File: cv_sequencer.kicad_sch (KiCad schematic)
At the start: 27 parts, among them J10 3096_USBC_RA_SMD, J11 4005_SWD_Header, J9 3086_Connector_Eurorack_Power, U1 3097_TFT_Display_SPI, U2 3093_MIC5225_3v3, U3 4002_RP2040, Y1 4004-Crystal-12MHz_GND24

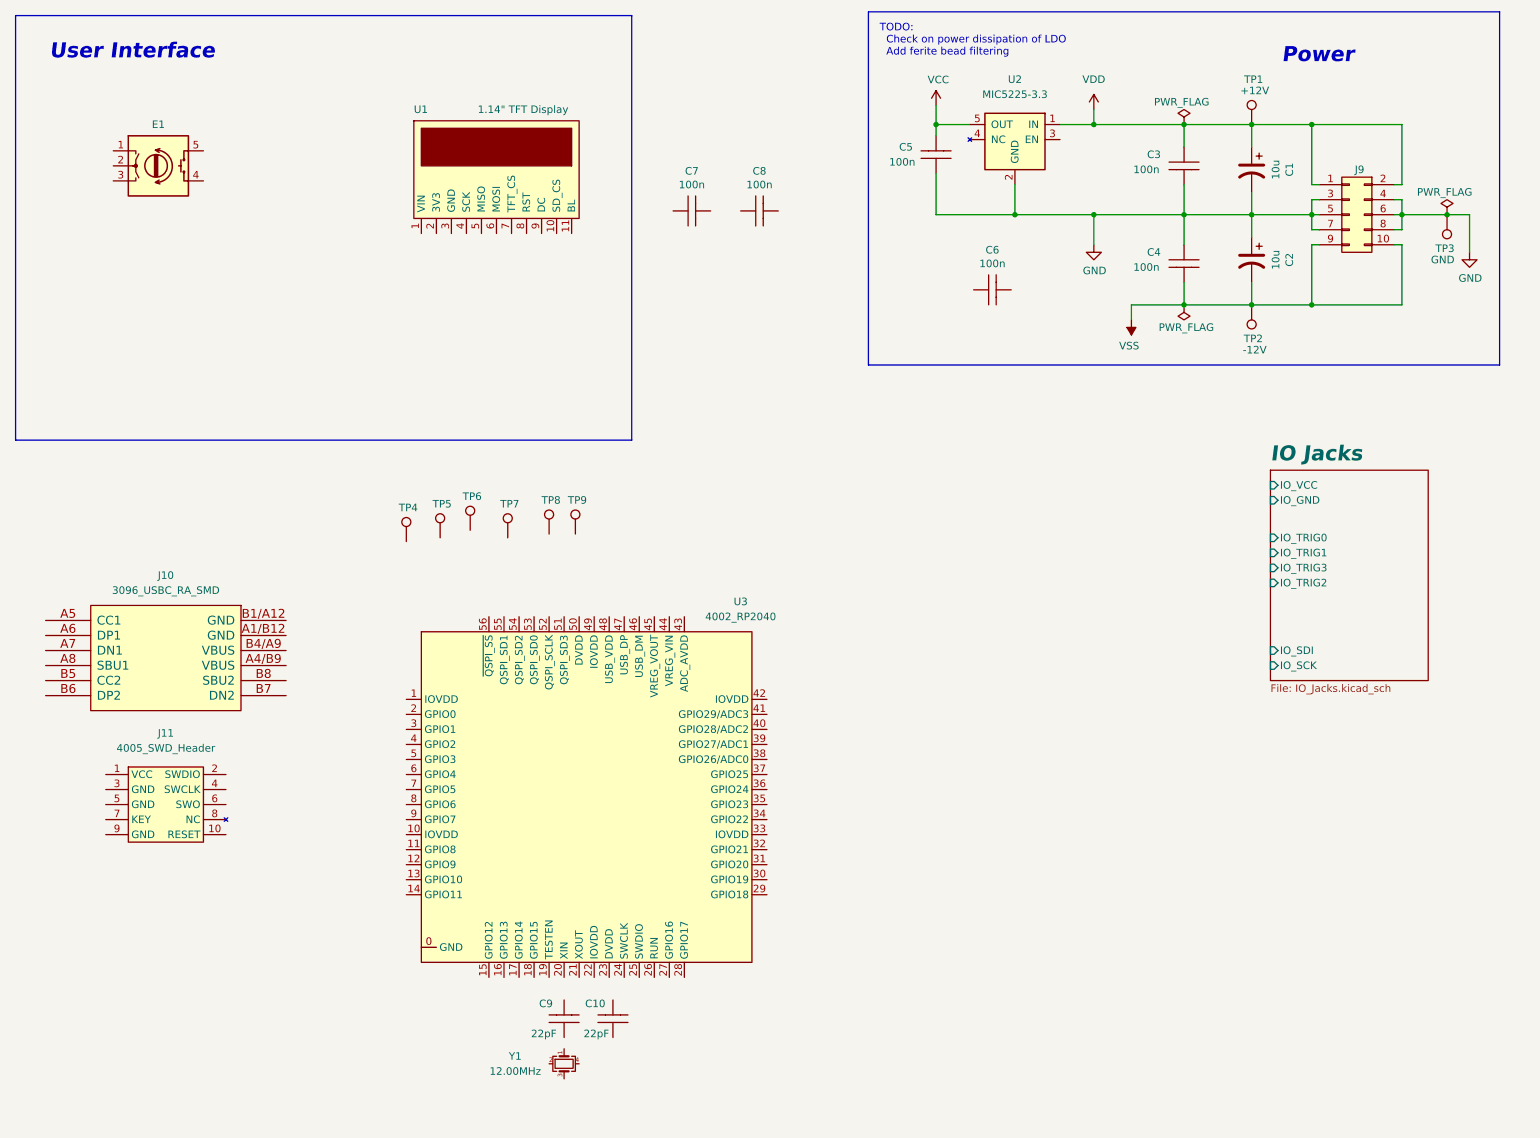
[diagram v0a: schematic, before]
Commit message: fleshed out a lot of the MCU circuitry
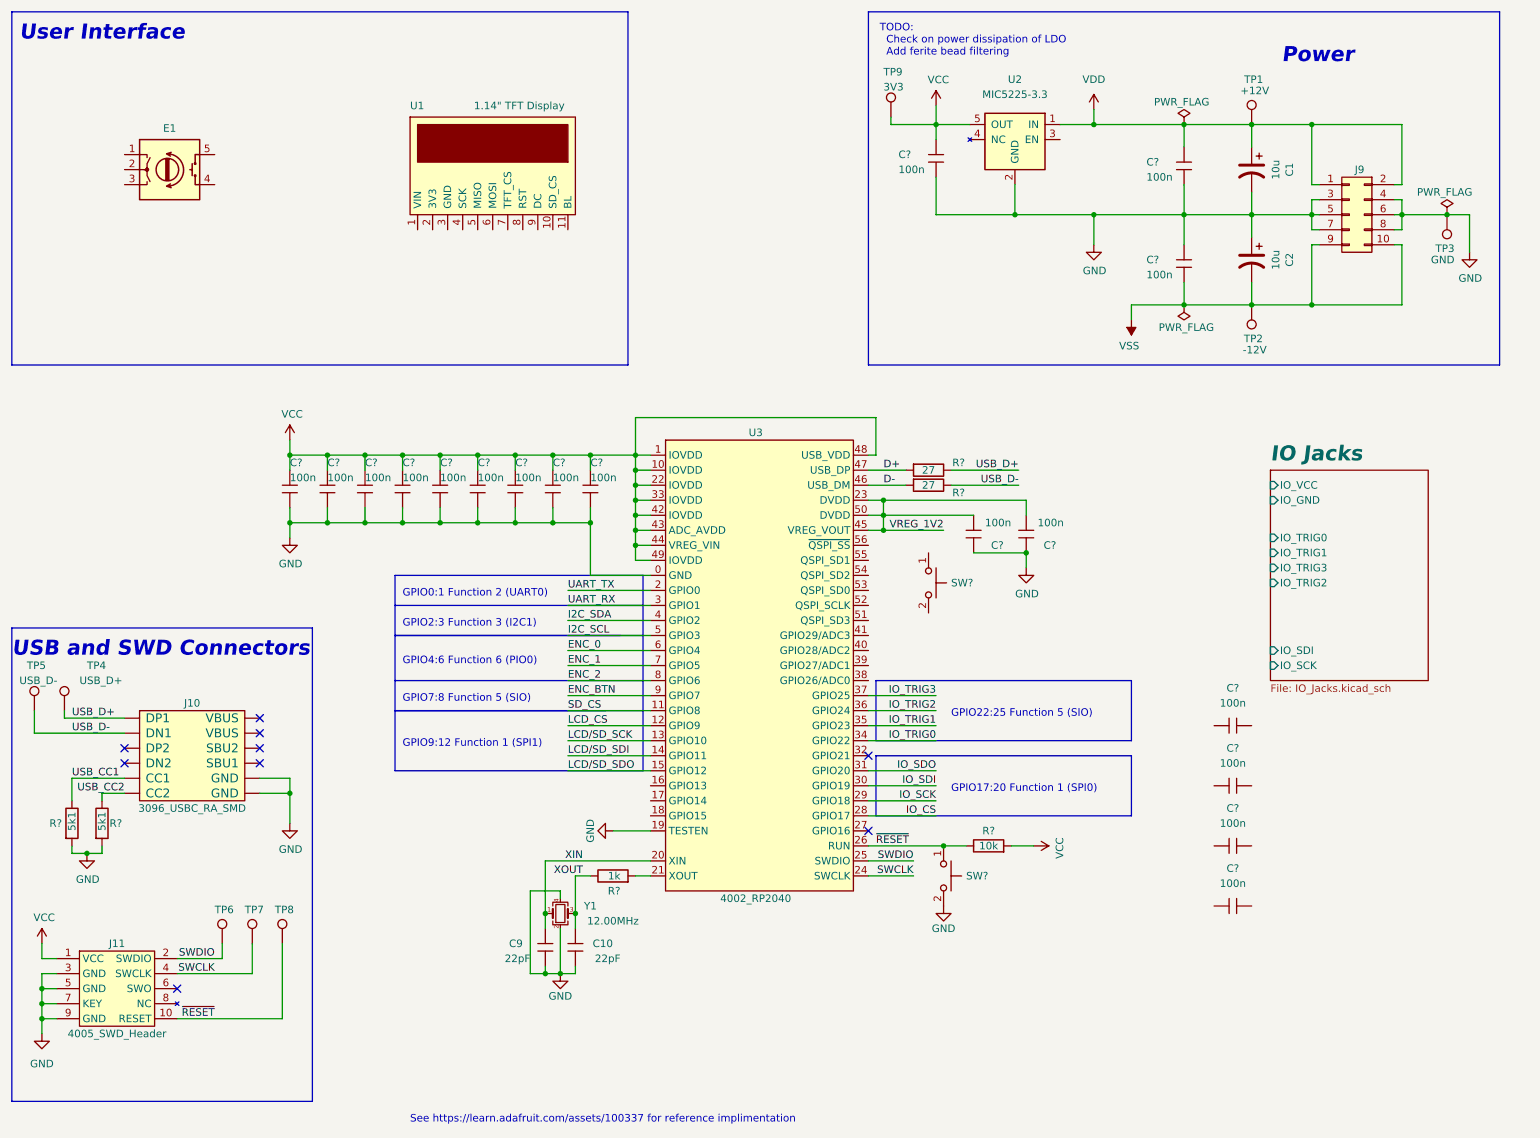
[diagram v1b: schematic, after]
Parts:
- removed C3, C4, C5, C6, C7, C8: 3089_Capacitor_100n_16V_SMD, Shulltronics_Generics:C_0402_HandSolder, symbol Shulltronics_Passives:3089_Capacitor_100n_16V_SMD
- added C? (x18): 3089_Capacitor_100n_16V_0402, Shulltronics_Generics:C_0402_HandSolder, symbol Shulltronics_Passives:3089_Capacitor_100n_16V_0402
- added R? (x2): 4009_Resistor_SMD_5k1_0.10W_1%, Shulltronics_Passives:Resistor_0402, symbol Shulltronics_Passives:4009_Resistor_SMD_5k1_0.10W_1%
- added R? (x2): 4011_Resistor_SMD_27_0.125W_1%, Shulltronics_Passives:Resistor_0402, symbol Shulltronics_Passives:4011_Resistor_SMD_27_0.125W_1%
- added R?: 4008_Resistor_SMD_10k_0.125W_1%, Shulltronics_Passives:Resistor_0402, symbol Shulltronics_Passives:4008_Resistor_SMD_10k_0.125W_1%
- added R?: 4010_Resistor_SMD_1k_0.125W_1%, Shulltronics_Passives:Resistor_0402, symbol Shulltronics_Passives:4010_Resistor_SMD_1k_0.125W_1%
- added SW? (x2): 4012_PushButton_NO_SMD, Shulltronics_ElectroMechanical:4012_PushButton_NO_SMD, symbol Shulltronics_ElectroMechanical:4012_PushButton_NO_SMD
- TP4: value TestPoint -> USB_D+
- TP5: value TestPoint -> USB_D-
- TP9: value TestPoint -> 3V3
- U3: SPN (none) -> 4002
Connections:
- net GND: now also C10.1, C9.1, J10.A1/B12 (GND), J10.B1/A12 (GND), J11.3 (GND), J11.5 (GND), J11.7 (KEY), J11.9 (GND), U3.0 (GND), U3.19 (TESTEN), Y1.2, Y1.4, C?.1, C?.1, C?.1, C?.1, C?.1, C?.1, C?.1, C?.1, C?.1, C?.1, C?.1, C?.2, C?.2, C?.2, R?.2, R?.2, SW?.2
- net VCC: now also J11.1 (VCC), TP9.1, U3.1 (IOVDD), U3.10 (IOVDD), U3.22 (IOVDD), U3.33 (IOVDD), U3.42 (IOVDD), U3.43 (ADC_AVDD), U3.44 (VREG_VIN), U3.48 (USB_VDD), U3.49 (IOVDD), C?.2, C?.2, C?.2, C?.2, C?.2, C?.2, C?.2, C?.2, C?.2, C?.2, R?.2
- net VDD: now also C?.2
- net VSS: now also C?.1
- net USB_D+: now reaches TP4.1
- net USB_D+: now also J10.A6 (DP1), R?.1
- net ~{RESET}: now reaches TP8.1
- net ~{RESET}: now also J11.10 (RESET), U3.26 (RUN), R?.1, SW?.1
- net USB_CC1: now reaches J10.A5 (CC1)
- net USB_CC1: now also R?.1
- net USB_D-: now reaches J10.A7 (DN1)
- net USB_D-: now also TP5.1, R?.1
- net USB_CC2: now reaches J10.B5 (CC2)
- net USB_CC2: now also R?.1
- net XIN: now reaches Y1.1
- net XIN: now also C9.2, U3.20 (XIN)
- net XOUT: now reaches Y1.3
- net XOUT: now also C10.2, R?.1
- net SWDIO: now reaches TP6.1
- net SWDIO: now also J11.2 (SWDIO), U3.25 (SWDIO)
- net SWCLK: now reaches J11.4 (SWCLK)
- net SWCLK: now also TP7.1, U3.24 (SWCLK)
- net SD_CS: now reaches U3.11 (GPIO8)
- net LCD_CS: now reaches U3.12 (GPIO9)
- net LCD/SD_SCK: now reaches U3.13 (GPIO10)
- net LCD/SD_SDI: now reaches U3.14 (GPIO11)
- net LCD/SD_SDO: now reaches U3.15 (GPIO12)
- net UART_TX: now reaches U3.2 (GPIO0)
- net at U3.21 (XOUT): now also R?.2
- net VREG_1V2: now reaches U3.23 (DVDD)
- net VREG_1V2: now also U3.45 (VREG_VOUT), U3.50 (DVDD), C?.1, C?.1
- net IO_CS: now reaches U3.28 (GPIO17)
- net IO_SCK: now reaches U3.29 (GPIO18)
- net UART_RX: now reaches U3.3 (GPIO1)
- net IO_SDI: now reaches U3.30 (GPIO19)
- net IO_SDO: now reaches U3.31 (GPIO20)
- net IO_TRIG0: now reaches U3.34 (GPIO22)
- net IO_TRIG1: now reaches U3.35 (GPIO23)
- net IO_TRIG2: now reaches U3.36 (GPIO24)
- net IO_TRIG3: now reaches U3.37 (GPIO25)
- net I2C_SDA: now reaches U3.4 (GPIO2)
- net D-: now reaches U3.46 (USB_DM)
- net D-: now also R?.2
- net D+: now reaches U3.47 (USB_DP)
- net D+: now also R?.2
- net I2C_SCL: now reaches U3.5 (GPIO3)
- net ENC_0: now reaches U3.6 (GPIO4)
- net ENC_1: now reaches U3.7 (GPIO5)
- net ENC_2: now reaches U3.8 (GPIO6)
- net ENC_BTN: now reaches U3.9 (GPIO7)
- no-connect marks 0 -> 9
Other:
- note added: "GPIO0:1 Function 2 (UART0)"
- note added: "GPIO17:20 Function 1 (SPI0)"
- note added: "GPIO22:25 Function 5 (SIO)"
- note added: "GPIO2:3 Function 3 (I2C1)"
- note added: "GPIO4:6 Function 6 (PIO0)"
- note added: "GPIO7:8 Function 5 (SIO)"
- note added: "GPIO9:12 Function 1 (SPI1)"
- note added: "See https://learn.adafruit.com/assets/100337 for reference implimentation"
- note added: "USB and SWD Connectors"
- moved on the sheet: E1, J11, TP4, TP5, TP6, TP7, TP8, TP9, U1, U3, Y1

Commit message: worked on gate input circuitry
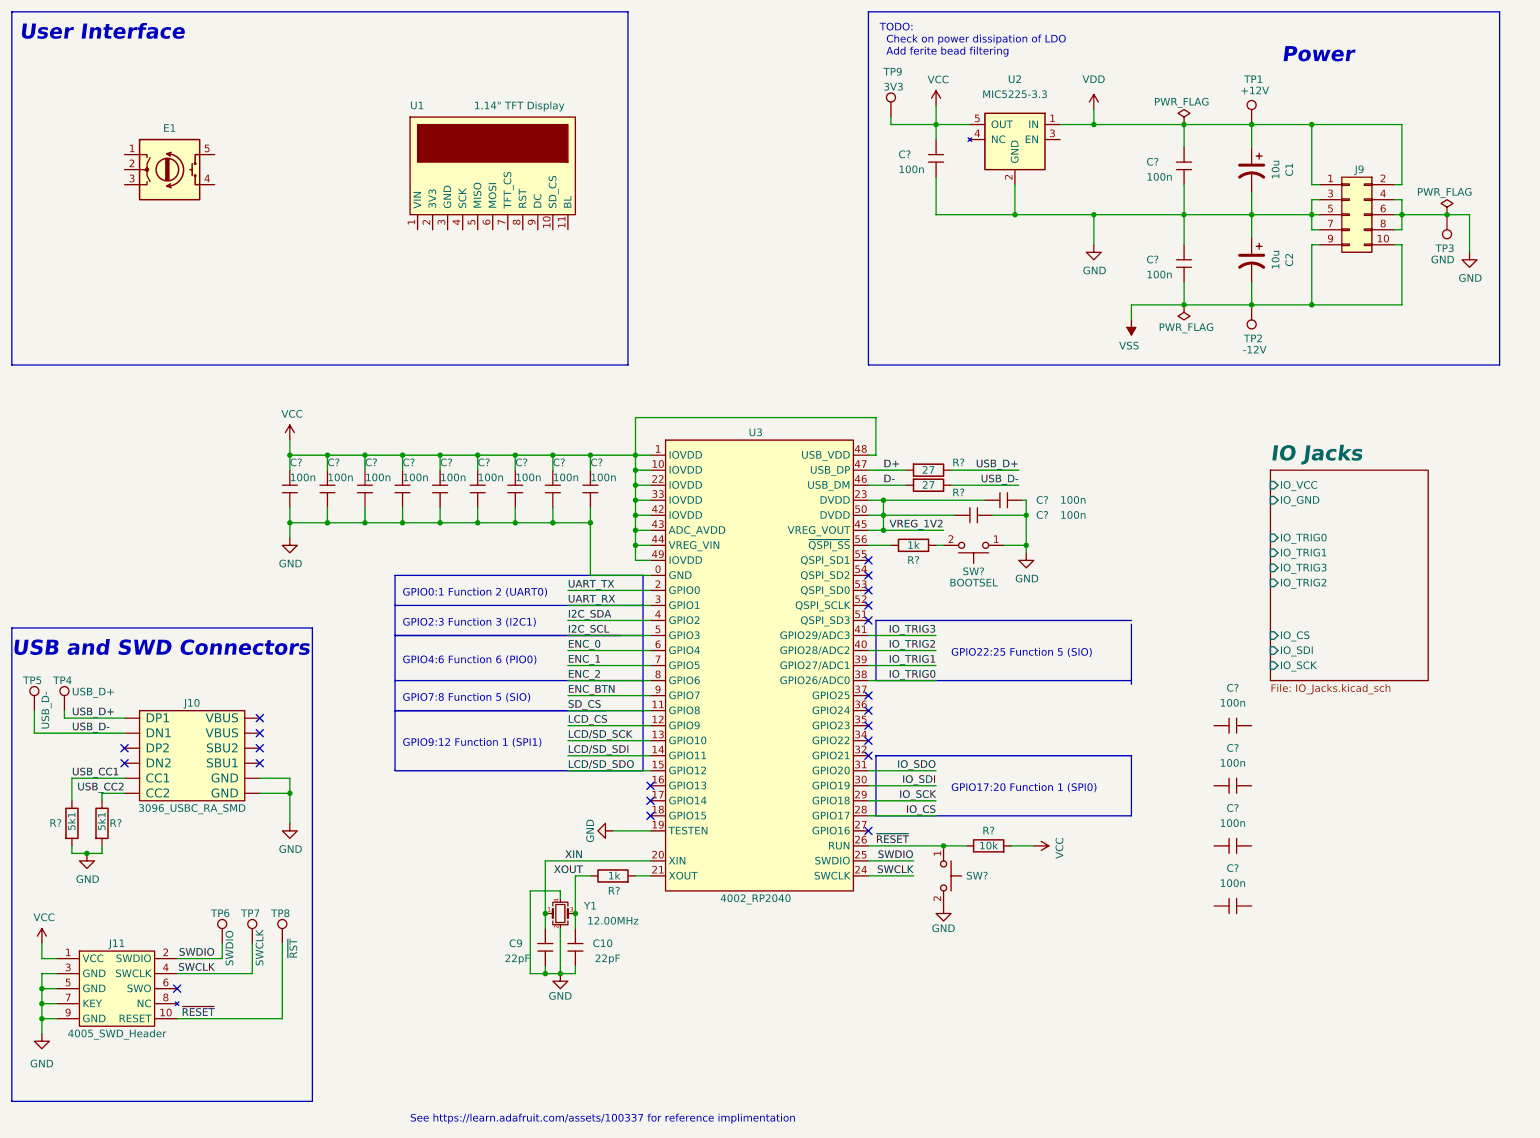
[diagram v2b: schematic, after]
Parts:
- added R?: 4010_Resistor_SMD_1k_0.125W_1%, Shulltronics_Passives:Resistor_0402, symbol Shulltronics_Passives:4010_Resistor_SMD_1k_0.125W_1%
- SW?: value 4012_PushButton_NO_SMD -> BOOTSEL
- TP6: value TestPoint -> SWDIO
- TP7: value TestPoint -> SWCLK
- TP8: value TestPoint -> ~{RST}
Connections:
- net GND: now also SW?.1
- net IO_TRIG0: now also U3.38 (GPIO26/ADC0); no longer U3.34 (GPIO22)
- net IO_TRIG1: now also U3.39 (GPIO27/ADC1); no longer U3.35 (GPIO23)
- net IO_TRIG2: now also U3.40 (GPIO28/ADC2); no longer U3.36 (GPIO24)
- net IO_TRIG3: now also U3.41 (GPIO29/ADC3); no longer U3.37 (GPIO25)
- net at SW?.2: now also R?.2
- net at U3.56 (~{QSPI_SS}): now also R?.1
- no-connect marks 9 -> 21
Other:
- sheet IO Jacks ports: added IO_CS; removed none
- moved on the sheet: C?, SW?
